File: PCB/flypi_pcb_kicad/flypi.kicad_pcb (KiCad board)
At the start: 2 copper layers, 76 x 93 mm, 44 parts, among them CON1 BARREL_JACK, P1 PeltS1S2, P10 RGB RG-B, P2 Pi+-, P3 Fan-+, P4 Therm +s-, P5 HP1-+, P6 HP2-+, P7 servo -s+, P8 Ring s-+, P9 matrix sdsc-+, Q1 1A_NPN_ECB, Q2 1A-NPN-ECB, Q3 1A_NPN_ECB, Q4 1A_NPN_ECB, U1 LM2596, U2 LM2596, U3 LM2596, U4 L298N, U5 arduino_mini

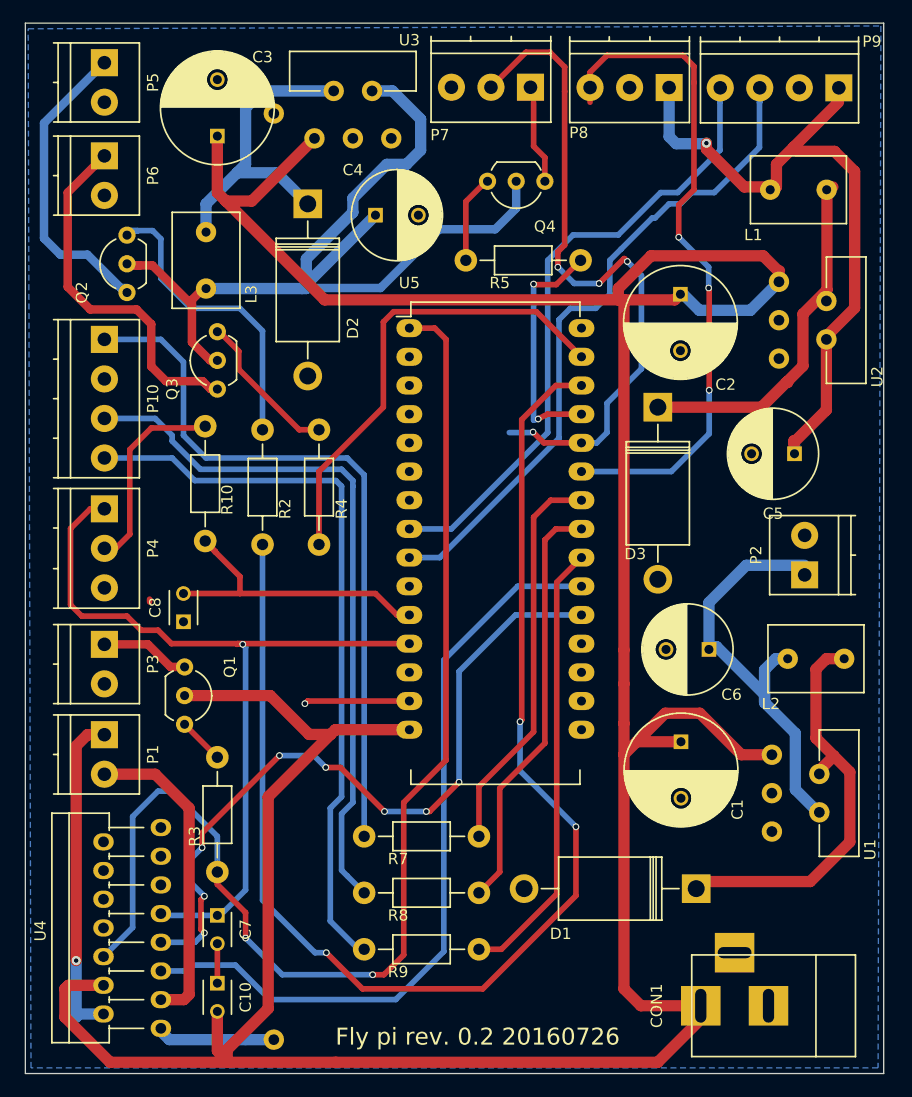
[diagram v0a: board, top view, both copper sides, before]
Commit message: bring all updates from Prometheus development to original repo (#25)
* small corrections to the timing address for LEDs

* first change on the protocol class

* added schematics for electronics, python code and overall components

* updated gerber files

* updated BOM

* last chages tryig to fix protocol

* see to have found the problem and solutio for the protocol app. System now is bidirectional. Pytho sends command and waits for done cofirmation from arduino

* more development on the protocol class

* arduino commit

* app commit

* protol commit

* turned off a few classes

* finally fixed protocol bug.

* added peltier to protocol

* horizontal and vertical offsets start in the middle of the frame

* implemented zap for leds

* small bugfix for the wuit app

* initial commit to start recording to the protocol class

* finished implementing camera recording for protocol

* implemented code in protocol class

* finished implementing conversion to protocol class. but conversion takes too long.

* transformed the conversion code into a button callback. So the user needs to manually convert the videos. This is done because conversion can take a long time and prevent user from doing experiments. Also updated the conversion code itself into something that seems to work

* updated readme to include installation steps for libav-tools

* small changes to the files to be 3d printed

* microfluidic chamber holder.

* turned all classes on

* added pychache to gitignore

* recreated mockup class

* increased tolerance on print files to print with 0.8 nozzle

* added another pattern for the matrix and set the arduino function for it to a long matrix.

* added user and assembly manual

* added custom background image

* update gitignore

* repo clean uo, moving old and unused files to specific folders

* removing old files

* add new bill of materials

* update camholder for picamera v2

* Fix README t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
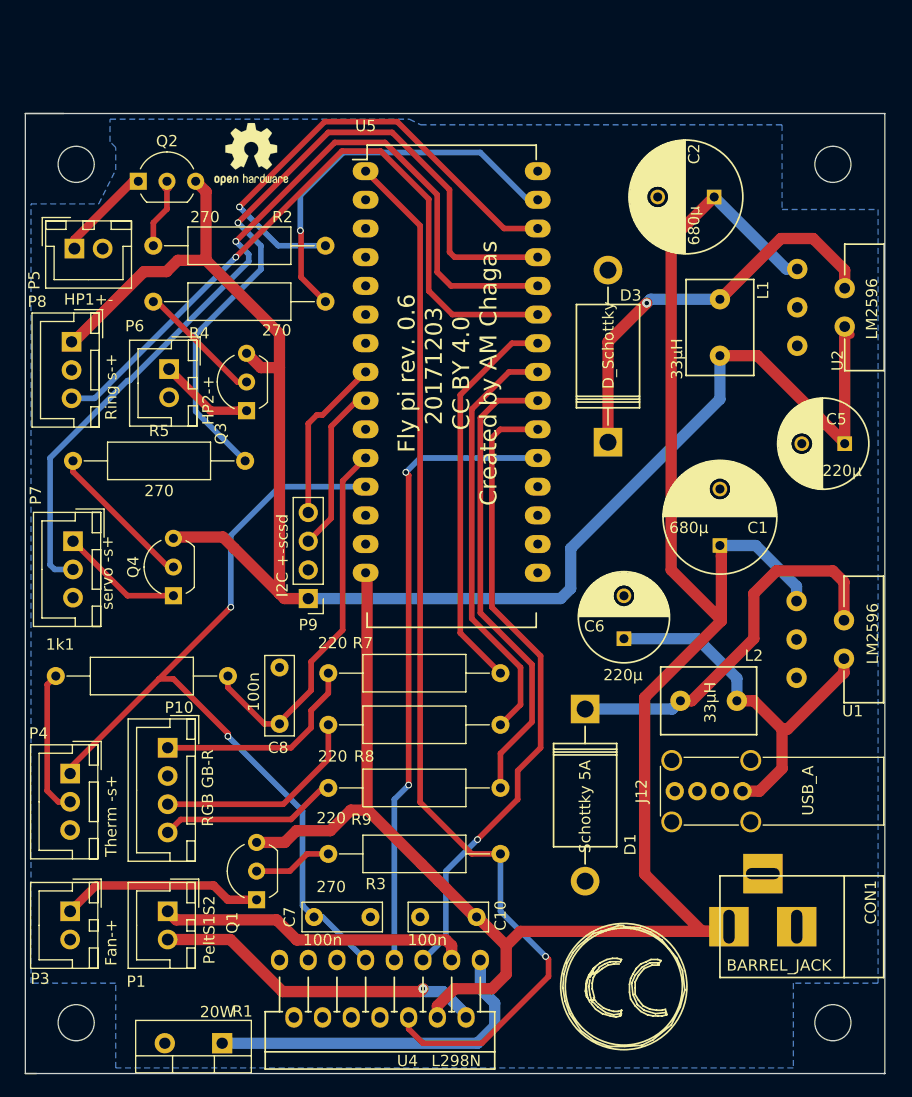
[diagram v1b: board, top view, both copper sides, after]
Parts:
- removed C3: 680µ, Capacitors_ThroughHole:C_Radial_D10_L21_P5
- removed C4: 220µ, Capacitors_ThroughHole:C_Radial_D8_L13_P3.8
- removed D2: Schottky 5A, Diodes_ThroughHole:Diode_DO-201AD_Horizontal_RM15
- removed L3: 33µH, Inductors_NEOSID:Neosid_Inductor_MA-Bs75
- removed P2: Pi+-, Terminal_Blocks:TerminalBlock_Pheonix_PT-3.5mm_2pol
- removed R10: 1k, Resistors_ThroughHole:Resistor_Horizontal_RM10mm
- removed U3: LM2596, footprints:LM2596
- added  : , Mounting_Holes:MountingHole_3.2mm_M3_DIN965, F.Cu at (109.5, 53.5)
- added 1k1: R, Resistors_THT:R_Axial_DIN0309_L9.0mm_D3.2mm_P15.24mm_Horizontal, F.Cu at (122.9, 98.8)
- added ?: , Mounting_Holes:MountingHole_3.2mm_M3_DIN965, F.Cu at (109.5, 129.5)
- added ?: , Mounting_Holes:MountingHole_3.2mm_M3_DIN965, F.Cu at (176.5, 53.5)
- added ?: , Symbols:OSHW-Logo2_7.3x6mm_SilkScreen, F.Cu at (125.0, 52.6)
- added ?: , Symbols:Symbol_CreativeCommons_SilkScreenTop_Type2_Big, F.Cu at (158.0, 126.3)
- added ?: , Mounting_Holes:MountingHole_3.2mm_M3_DIN965, F.Cu at (176.5, 129.5)
- added J12: USB_A, Connectors:USB_A_Vertical, F.Cu at (168.5, 109.0)
- C10, C7: footprint Capacitors_ThroughHole:C_Disc_D3_P2.5 -> Capacitors_THT:C_Rect_L7.0mm_W2.5mm_P5.00mm
- C8: value 0.1µ -> 100n; footprint Capacitors_ThroughHole:C_Disc_D3_P2.5 -> Capacitors_THT:C_Rect_L7.0mm_W2.5mm_P5.00mm
- P1, P3, P6: footprint Terminal_Blocks:TerminalBlock_Pheonix_PT-3.5mm_2pol -> Connectors_JST:JST_XH_B02B-XH-A_02x2.50mm_Straight
- P10: value RGB RG-B -> RGB GB-R; footprint Terminal_Blocks:TerminalBlock_Pheonix_PT-3.5mm_4pol -> Connectors_JST:JST_XH_B04B-XH-A_04x2.50mm_Straight
- P4: value Therm +s- -> Therm -s+; footprint Terminal_Blocks:TerminalBlock_Pheonix_PT-3.5mm_3pol -> Connectors_JST:JST_XH_B03B-XH-A_03x2.50mm_Straight
- P5: value HP1-+ -> HP1+-; footprint Terminal_Blocks:TerminalBlock_Pheonix_PT-3.5mm_2pol -> Connectors_JST:JST_XH_B02B-XH-A_02x2.50mm_Straight
- P7, P8: footprint Terminal_Blocks:TerminalBlock_Pheonix_PT-3.5mm_3pol -> Connectors_JST:JST_XH_B03B-XH-A_03x2.50mm_Straight
- P9: value matrix sdsc-+ -> I2C +-scsd; footprint Terminal_Blocks:TerminalBlock_Pheonix_PT-3.5mm_4pol -> Socket_Strips:Socket_Strip_Straight_1x04_Pitch2.54mm
- Q1, Q3, Q4: value 1A_NPN_ECB -> 1A_NPN_EBC
- Q2: value 1A-NPN-ECB -> 1A-NPN-EBC
- R1: value 1 - 18W -> 20W; footprint footprints:high_load_res -> TO_SOT_Packages_THT:TO-220-2_Vertical; moved to F.Cu
- R2, R3, R4, R5, R7, R8, R9: footprint Resistors_ThroughHole:Resistor_Horizontal_RM10mm -> Resistors_THT:R_Axial_DIN0309_L9.0mm_D3.2mm_P15.24mm_Horizontal
- moved P9 65.2 mm to (130.0, 91.9)
- moved P8 57.5 mm to (109.1, 69.2), turned to 270 degrees
- moved P7 57.1 mm to (109.2, 86.9), turned to 270 degrees
- moved Q4 49.3 mm to (118.1, 91.7), turned to 90 degrees
- moved R1 41.6 mm to (122.4, 131.3), turned to 180 degrees
- moved R5 39.1 mm to (109.2, 79.8)
- moved P10 36.6 mm to (117.6, 105.2)
- moved U4 28.9 mm to (145.3, 124.0), turned to 180 degrees
- moved P3 23.8 mm to (109.0, 119.6)
- moved P4 23.6 mm to (109.0, 107.4)
- moved Q1 21.6 mm to (125.5, 118.6), turned to 90 degrees
- moved P6 19.7 mm to (117.7, 71.6)
- moved R2 18.9 mm to (116.3, 60.7), turned to 0 degrees
- moved C10 18.9 mm to (140.0, 120.1), turned to 0 degrees
- moved D1 18.7 mm to (154.6, 101.7), turned to 270 degrees
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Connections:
- Q1 pad 2: Net-(C1-Pad1) -> Net-(Q1-Pad2)
- Q1 pad 3: Net-(Q1-Pad3) -> Net-(C1-Pad1)
- Q2 pad 2: Net-(C4-Pad1) -> Net-(Q2-Pad2)
- Q2 pad 3: Net-(Q2-Pad3) -> Net-(C5-Pad1)
- Q3 pad 2: Net-(C4-Pad1) -> Net-(Q3-Pad2)
- Q3 pad 3: Net-(Q3-Pad3) -> Net-(C5-Pad1)
- Q4 pad 2: Net-(C4-Pad1) -> Net-(Q4-Pad2)
- Q4 pad 3: Net-(Q4-Pad3) -> Net-(C5-Pad1)
- R1 pad 1: GND -> Net-(R1-Pad1)
- R1 pad 2: Net-(R1-Pad2) -> GND
- R2 pad 1: Net-(Q2-Pad3) -> Net-(Q2-Pad2)
- R3 pad 1: Net-(Q1-Pad3) -> Net-(Q1-Pad2)
- R4 pad 1: Net-(Q3-Pad3) -> Net-(Q3-Pad2)
- R5 pad 1: Net-(Q4-Pad3) -> Net-(Q4-Pad2)
- U4 pad 1: Net-(R1-Pad2) -> Net-(R1-Pad1)
- U4 pad 2: Net-(P1-Pad1) -> Net-(P1-Pad2)
- U4 pad 3: Net-(P1-Pad2) -> Net-(P1-Pad1)
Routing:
- net Net-(C1-Pad1): track 302.0 -> 182.8 mm
- net Net-(C5-Pad1): track 60.2 -> 147.7 mm, vias 1 -> 0
- net Net-(C4-Pad1): track 84.4 -> 0.00 mm
- net Net-(R2-Pad2): track 116.9 -> 42.5 mm, vias 3 -> 1
- net Net-(P10-Pad4): track 65.0 -> 15.9 mm
- net Net-(P10-Pad1): track 63.8 -> 18.9 mm
- net Net-(P9-Pad3): track 59.2 -> 15.0 mm
- net Net-(P10-Pad3): track 62.3 -> 18.9 mm
- net Net-(R5-Pad2): track 21.5 -> 63.8 mm, vias 2 -> 1
- net Net-(P9-Pad4): track 55.9 -> 14.8 mm
- net Net-(R1-Pad1): track 0.00 -> 31.1 mm
- net Net-(D2-Pad1): track 28.3 -> 0.00 mm
- net Net-(Q2-Pad3): track 27.6 -> 0.00 mm
- net Net-(P6-Pad1): track 32.4 -> 9.08 mm
- net Net-(P5-Pad1): track 28.3 -> 8.59 mm
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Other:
- board size 76 x 93 mm -> 76.1 x 85 mm
- board text added: "Fly pi rev. 0.6 20171203 CC BY 4.0 Created by AM Chagas"
- board text added: "top"
- board text added: "www.prometheus-science.com https://github.com/prometheus-science/Flypi"
- board text removed: "Fly pi rev. 0.2 20160726"

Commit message: first implementation of the board being ported to KiCad5 and proper wiring of transistors
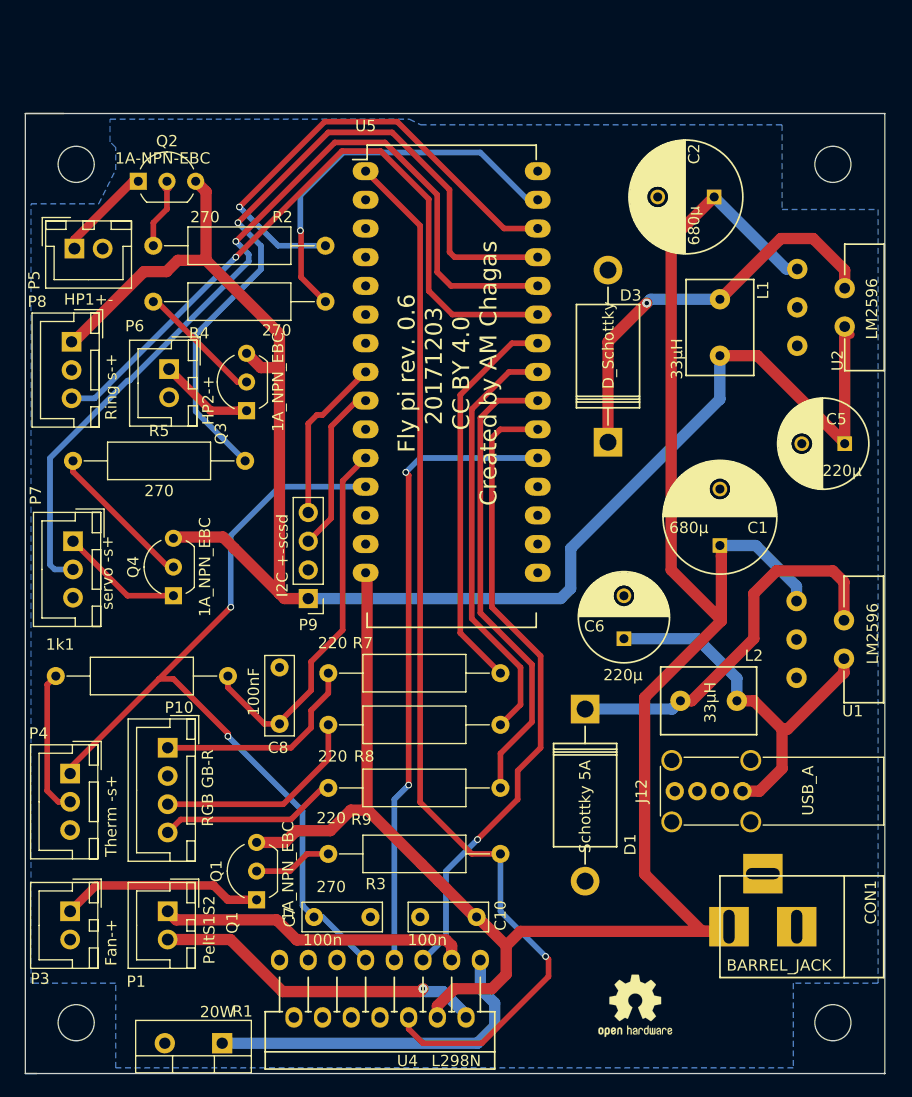
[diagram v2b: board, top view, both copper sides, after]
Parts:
- removed the ? at (158.0, 126.3)
- C8: value 100n -> 100nF
- moved ? 82.7 mm to (159.0, 128.0)
